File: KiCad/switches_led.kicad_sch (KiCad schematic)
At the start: 70 parts, among them Q2 MMBT3904, Q3 MMBT3904, Q4 MMBT3904, Q5 MMBT3904, Q6 MMBT3904, Q7 MMBT3904, Q8 MMBT3904, Q9 MMBT3904, U2 CD4017BE

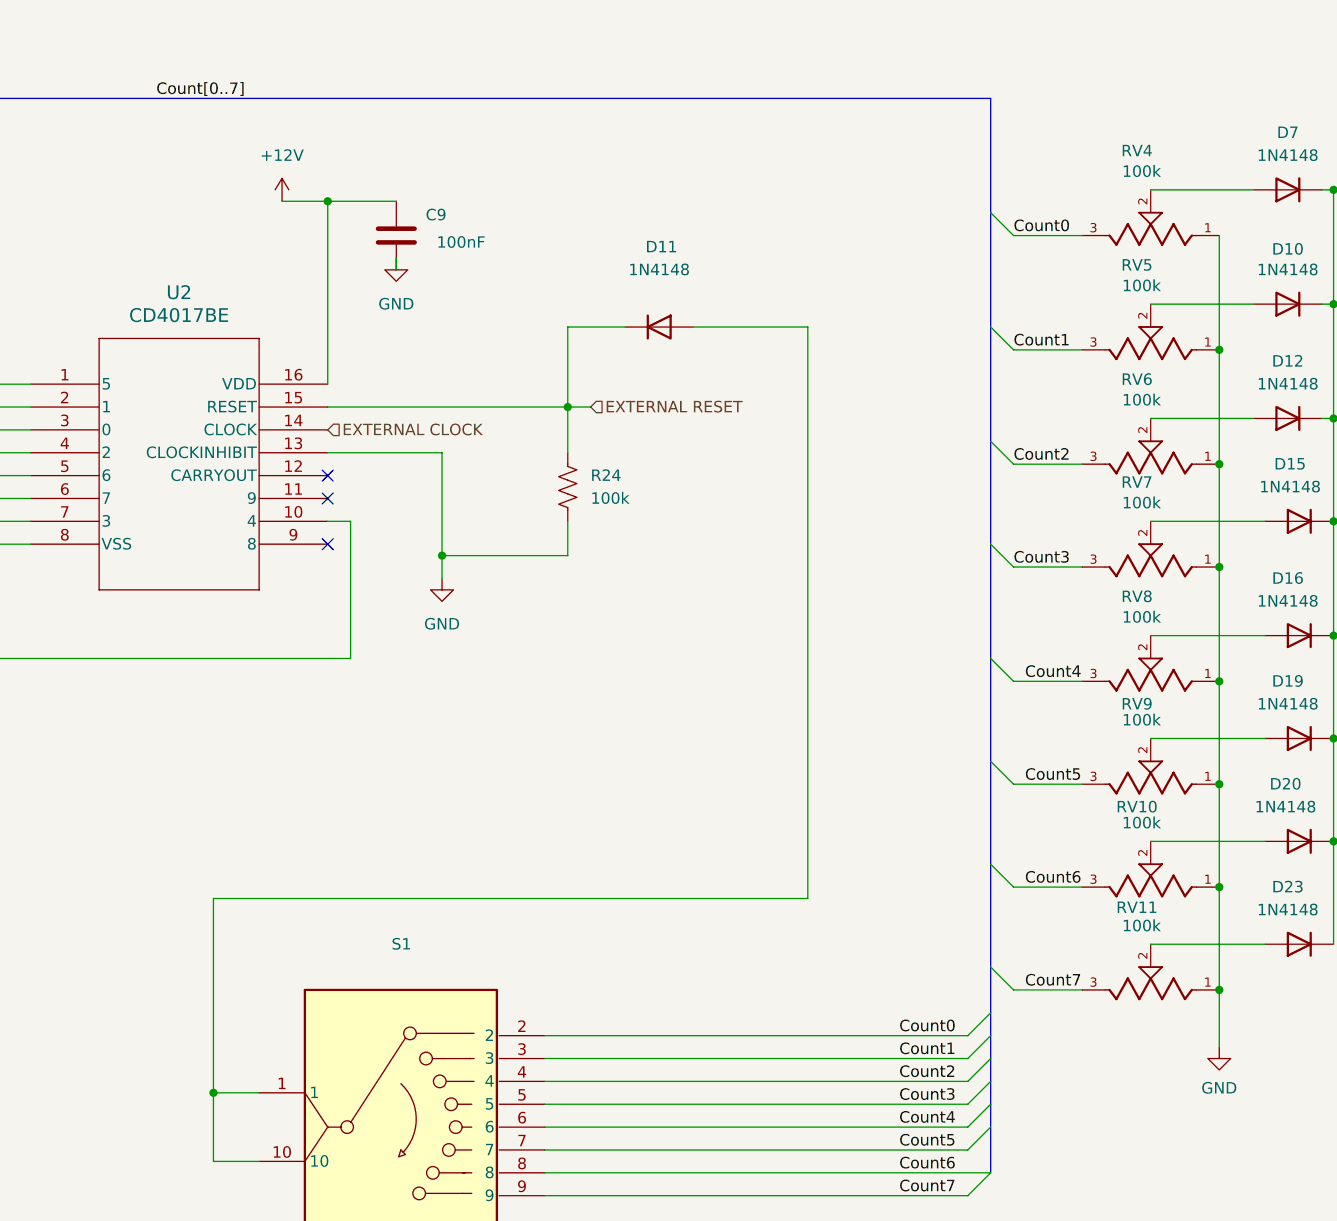
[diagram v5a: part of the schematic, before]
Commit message: re-placing components; optimizing text on silkscreen
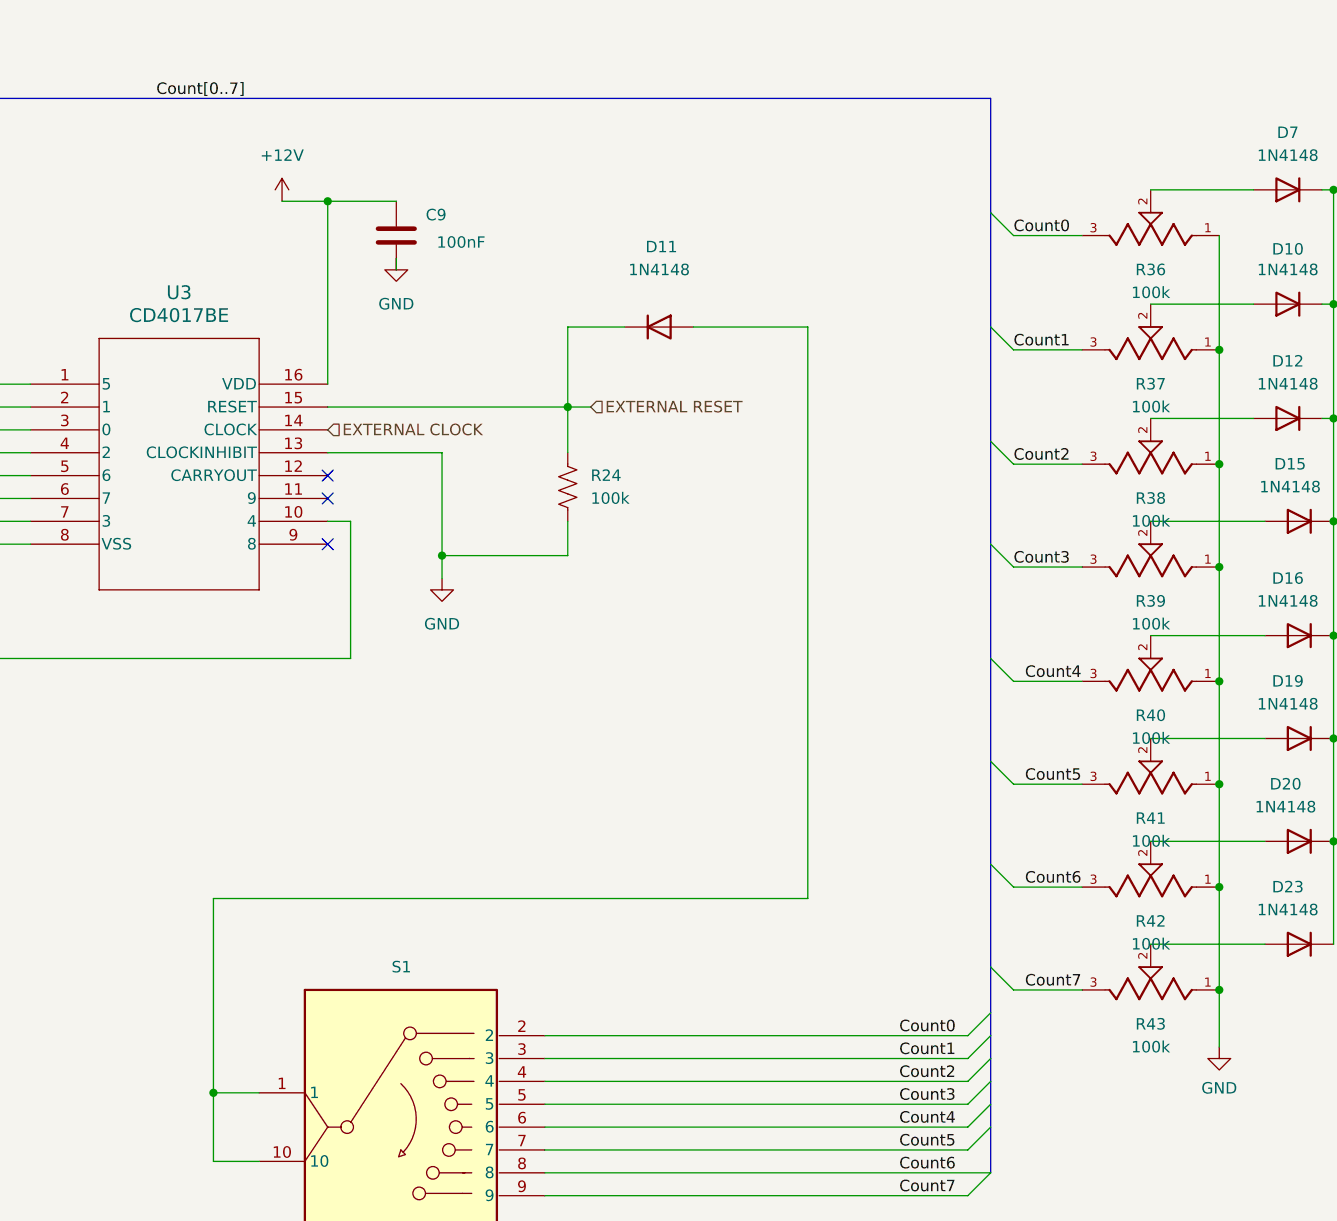
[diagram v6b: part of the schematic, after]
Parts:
- removed RV10, RV11, RV4, RV5, RV6, RV7, RV8, RV9: 100k, Eurorack:RD901F_1, symbol Eurorack:RD901F
- removed S1: SR1712F-0108-20F0A-N9-N-027, Eurorack:1 Pole 8 Step Switch Alpha, symbol Eurorack:SR1712F-0108-20F0A-N9-N-027
- removed U2: CD4017BE, Eurorack:CD4017BE THT, symbol Eurorack:CD4017BE
- added R36, R37, R38, R39, R40, R41, R42, R43: 100k, Eurorack:Potentiometer_Alpha_RD901F_Vertical_Alt, symbol Eurorack:Potentiometer_Alpha_RD901F_Vertical
- added S1: Switch_Rotary_Alpha_SR1712F_1P8T, Eurorack:Switch_Rotary_Alpha_SR1712F_1P8T, symbol Eurorack:Switch_Rotary_Alpha_SR1712F_1P8T
- added U3: CD4017BE, Eurorack:IC_DIP-16_CD4017BE_THT, symbol Eurorack:IC_DIP-16_CD4017BE_THT
- SW10, SW2, SW3, SW4, SW5, SW6, SW7, SW9: footprint Eurorack:2MS1T1B1M2QES -> Eurorack:Switch_Toggle_Dailywell_MS1T1B1M2QES_SPDT
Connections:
- net +12V: now also U3.16 (VDD)
- net Count0: now also R36.3, S1.2, U3.3 (0)
- net Count1: now also R37.3, S1.3, U3.2 (1)
- net Count2: now also R38.3, S1.4, U3.4 (2)
- net Count3: now also R39.3, S1.5, U3.7 (3)
- net Count4: now also R40.3, S1.6, U3.10 (4)
- net Count5: now also R41.3, S1.7, U3.1 (5)
- net Count6: now also R42.3, S1.8, U3.5 (6)
- net Count7: now also R43.3, S1.9, U3.6 (7)
- net EXTERNAL CLOCK: now also U3.14 (CLOCK)
- net EXTERNAL RESET: now also U3.15 (RESET)
- net GND: now also R36.1, R37.1, R38.1, R39.1, R40.1, R41.1, R42.1, R43.1, U3.13 (CLOCKINHIBIT), U3.8 (VSS)
- net at D11.2 (A): now also S1.1, S1.10
- net at D23.2 (A): now also R43.2
- net at D10.2 (A): now also R37.2
- net at D16.2 (A): now also R40.2
- net at D12.2 (A): now also R38.2
- net at D20.2 (A): now also R42.2
- net at D15.2 (A): now also R39.2
- net at D19.2 (A): now also R41.2
- net at D7.2 (A): now also R36.2

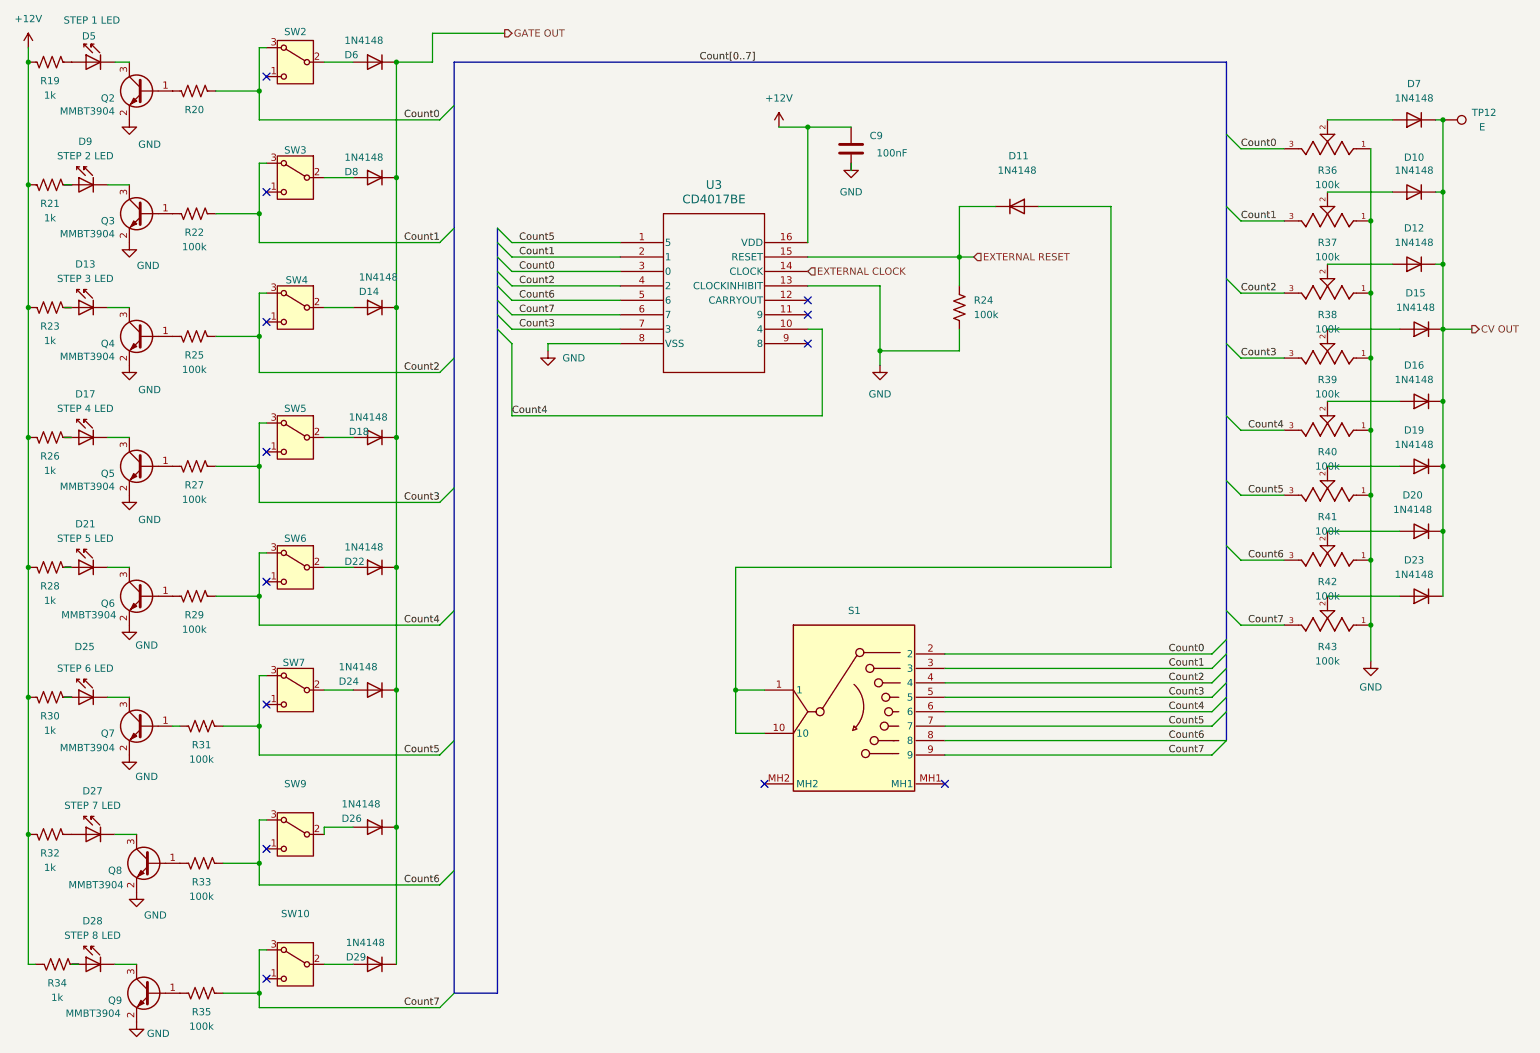
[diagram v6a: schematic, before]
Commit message: changing position on silkscreen
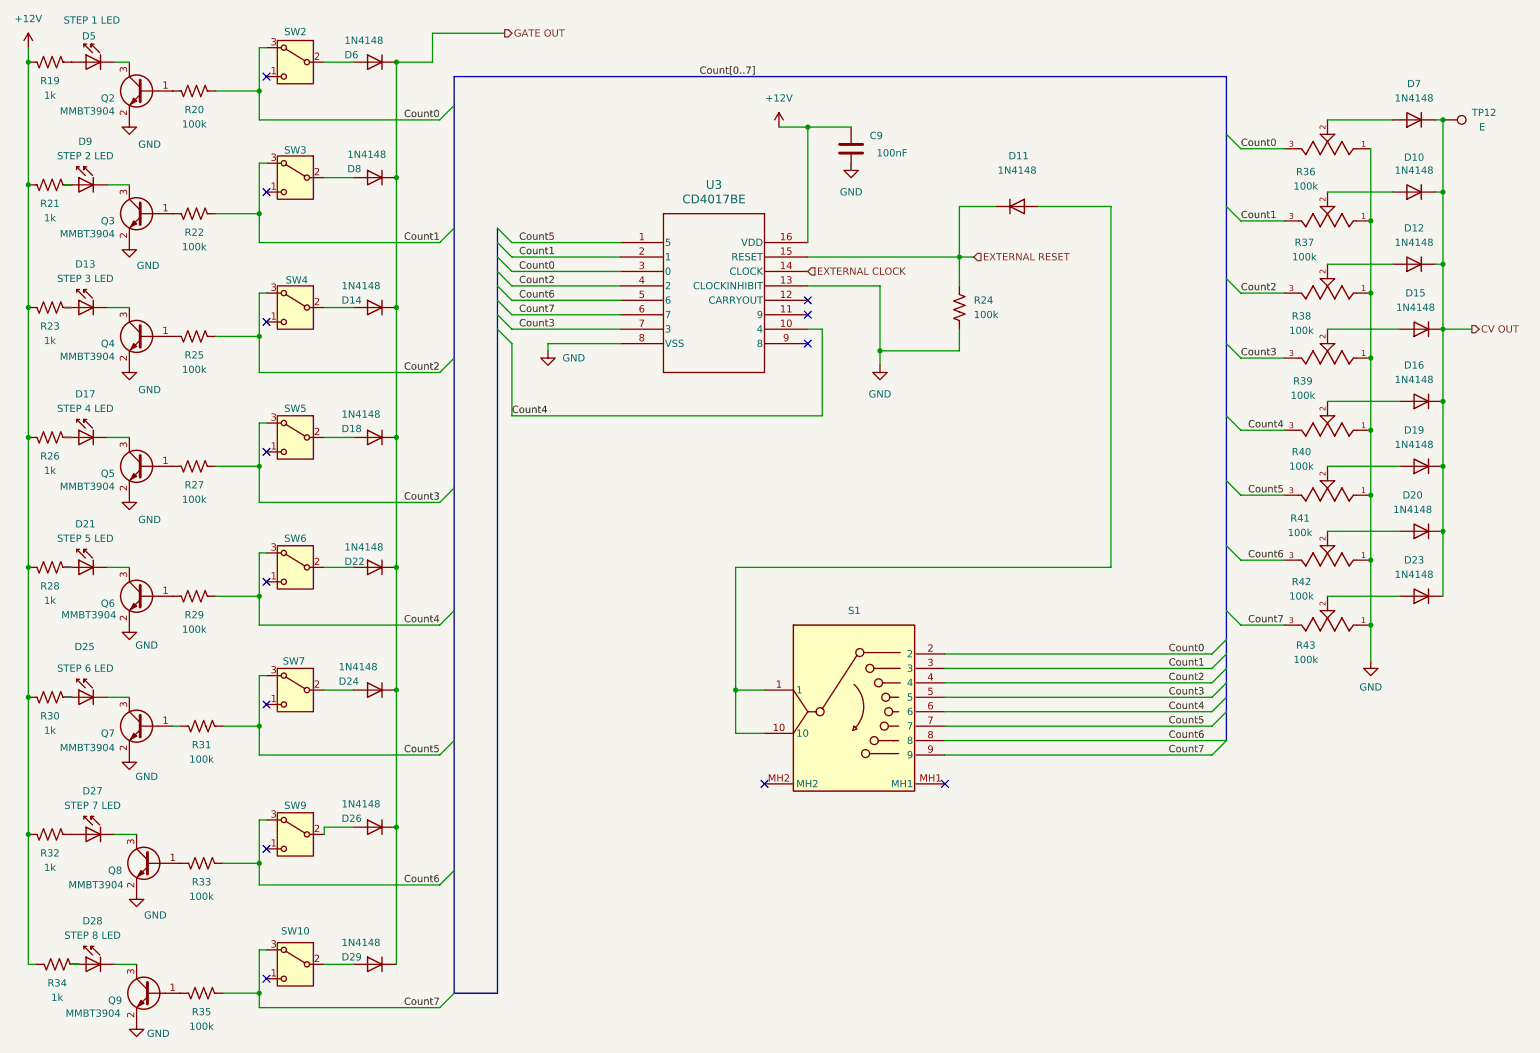
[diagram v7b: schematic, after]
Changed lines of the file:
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@@
 	(bus
 		(pts
-			(xy 93.98 24.13) (xy 229.87 24.13)
+			(xy 93.98 26.67) (xy 229.87 26.67)
 		)
 		(stroke
@@
 	(bus
 		(pts
-			(xy 229.87 24.13) (xy 229.87 36.83)
+			(xy 229.87 26.67) (xy 229.87 36.83)
 		)
 		(stroke
@@
 	(bus
 		(pts
-			(xy 93.98 24.13) (xy 93.98 31.75)
+			(xy 93.98 26.67) (xy 93.98 31.75)
 		)
 		(stroke
@@
 	)
 	(label "Count[0..7]"
-		(at 137.16 24.13 0)
+		(at 137.16 26.67 0)
 		(effects
 			(font
@@
 		(on_board yes)
 		(dnp no)
-		(fields_autoplaced yes)
 		(property "Reference" "R37"
-			(at 247.65 55.88 0)
+			(at 243.586 55.88 0)
 			(effects
 				(font
@@
 		)
 		(property "Value" "100k"
-			(at 247.65 58.42 0)
+			(at 243.586 58.42 0)
 			(effects
 				(font
@@
 		(dnp no)
 		(property "Reference" "D8"
-			(at 74.676 43.434 0)
+			(at 75.184 42.926 0)
 			(effects
 				(font
@@
 		)
 		(property "Value" "1N4148"
-			(at 74.676 40.894 0)
+			(at 75.184 40.386 0)
 			(effects
 				(font
@@
 		(dnp no)
 		(property "Reference" "SW9"
-			(at 66.04 151.13 0)
+			(at 66.04 154.94 0)
 			(effects
 				(font
@@
 		(on_board yes)
 		(dnp no)
-		(fields_autoplaced yes)
 		(property "Reference" "R43"
-			(at 247.65 127 0)
+			(at 243.84 126.746 0)
 			(effects
 				(font
@@
 		)
 		(property "Value" "100k"
-			(at 247.65 129.54 0)
+			(at 243.84 129.286 0)
 			(effects
 				(font
@@
 					(size 1.27 1.27)
 				)
-				(hide yes)
 			)
 		)
@@
 		(dnp no)
 		(property "Reference" "D29"
-			(at 74.93 181.61 0)
+			(at 74.168 181.61 0)
 			(effects
 				(font
@@
 		)
 		(property "Value" "1N4148"
-			(at 74.93 179.07 0)
+			(at 74.168 179.07 0)
 			(effects
 				(font
@@
 		(on_board yes)
 		(dnp no)
-		(fields_autoplaced yes)
 		(property "Reference" "R39"
-			(at 247.65 80.01 0)
+			(at 243.332 80.264 0)
 			(effects
 				(font
@@
 		)
 		(property "Value" "100k"
-			(at 247.65 82.55 0)
+			(at 243.332 82.804 0)
 			(effects
 				(font
@@
 		(dnp no)
 		(property "Reference" "D18"
-			(at 75.438 89.154 0)
+			(at 74.168 88.646 0)
 			(effects
 				(font
@@
 		)
 		(property "Value" "1N4148"
-			(at 75.438 86.614 0)
+			(at 74.168 86.106 0)
 			(effects
 				(font
@@
 		(on_board yes)
 		(dnp no)
-		(fields_autoplaced yes)
 		(property "Reference" "SW10"
-			(at 66.04 173.99 0)
+			(at 66.04 177.038 0)
 			(effects
 				(font
@@
 		(dnp no)
 		(property "Reference" "SW7"
-			(at 65.786 129.794 0)
+			(at 65.786 129.54 0)
 			(effects
 				(font
@@
 		(on_board yes)
 		(dnp no)
-		(fields_autoplaced yes)
 		(property "Reference" "R38"
-			(at 247.65 68.58 0)
+			(at 243.078 68.834 0)
 			(effects
 				(font
@@
 		)
 		(property "Value" "100k"
-			(at 247.65 71.12 0)
+			(at 243.078 71.374 0)
 			(effects
 				(font
@@
 		(on_board yes)
 		(dnp no)
-		(fields_autoplaced yes)
 		(property "Reference" "R40"
-			(at 247.65 92.71 0)
+			(at 243.078 92.71 0)
 			(effects
 				(font
@@
 		)
 		(property "Value" "100k"
-			(at 247.65 95.25 0)
+			(at 243.078 95.25 0)
 			(effects
 				(font
@@
 		(on_board yes)
 		(dnp no)
-		(fields_autoplaced yes)
 		(property "Reference" "R36"
-			(at 247.65 43.18 0)
+			(at 243.84 43.434 0)
 			(effects
 				(font
@@
 		)
 		(property "Value" "100k"
-			(at 247.65 45.72 0)
+			(at 243.84 45.974 0)
 			(effects
 				(font
@@
 		(on_board yes)
 		(dnp no)
-		(fields_autoplaced yes)
 		(property "Reference" "R41"
-			(at 247.65 104.14 0)
+			(at 242.824 104.394 0)
 			(effects
 				(font
@@
 		)
 		(property "Value" "100k"
-			(at 247.65 106.68 0)
+			(at 242.824 106.934 0)
 			(effects
 				(font
@@
 		(dnp no)
 		(property "Reference" "D14"
-			(at 77.216 64.516 0)
+			(at 74.168 66.04 0)
 			(effects
 				(font
@@
 		)
 		(property "Value" "1N4148"
-			(at 77.216 61.976 0)
+			(at 74.168 63.5 0)
 			(effects
 				(font
@@
 		(on_board yes)
 		(dnp no)
-		(fields_autoplaced yes)
 		(property "Reference" "R42"
-			(at 247.65 115.57 0)
+			(at 243.078 115.57 0)
 			(effects
 				(font
@@
 		)
 		(property "Value" "100k"
-			(at 247.65 118.11 0)
+			(at 243.078 118.11 0)
 			(effects
 				(font
